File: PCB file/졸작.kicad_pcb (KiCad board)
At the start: 2 copper layers, 7 parts

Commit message: change Pin
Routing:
- net GND: track 239.1 -> 461.2 mm, vias 3 -> 10
- net (no net): track 188.1 -> 18.8 mm, vias 7 -> 1
- net VCC: track 95.5 -> 128.1 mm, vias 0 -> 2

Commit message: Change PCB file
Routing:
- net (no net): track 18.8 -> 66.0 mm, vias 1 -> 0
- net GND: track 461.2 -> 444.9 mm, vias 10 -> 7
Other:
- board text removed: "10"
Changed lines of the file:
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@@
-	)
-	(gr_rect
-		(start 50.1 25.55)
-		(end 51.5 38.05)
-		(stroke
-			(width 0.1)
-			(type solid)
-		)
-		(fill no)
-		(layer "F.SilkS")
-	)
-	(gr_rect
-		(start 52.7 25.55)
-		(end 54.1 38.05)
-		(stroke
-			(width 0.1)
-			(type solid)
-		)
-		(fill no)
-		(layer "F.SilkS")
 	)
 	(gr_rect
@@
 		(layer "F.Paste")
 	)
-	(gr_text "10"
-		(at 52.35 31.625 0)
-		(layer "F.SilkS")
-		(effects
-			(font
-				(size 0.5 0.5)
-				(thickness 0.1)
-			)
-		)
+	(gr_rect
+		(start 49.6 26.2)
+		(end 54.6 29.2)
+		(stroke
+			(width 0.2)
+			(type solid)
+		)
+		(fill yes)
+		(layer "B.Paste")
+	)
+	(gr_rect
+		(start 49.6 30.7)
+		(end 54.6 33.7)
+		(stroke
+			(width 0.2)
+			(type solid)
+		)
+		(fill yes)
+		(layer "B.Paste")
 	)
 	(gr_text "VCC"
@@
 		)
 	)
+	(gr_text_box "PIN0\n"
+		(start 49.95 26.85)
+		(end 54.25 28.6)
+		(margins 1.0025 1.0025 1.0025 1.0025)
+		(layer "F.SilkS")
+		(effects
+			(font
+				(size 1 1)
+				(thickness 0.2)
+				(bold yes)
+			)
+			(justify mirror)
+		)
+		(border yes)
+		(stroke
+			(width 0.1)
+			(type dot)
+		)
+	)
 	(gr_text_box "B-"
 		(start 19.95 41.05)
@@
 		)
 	)
+	(gr_text_box "C-PWM"
+		(start 48.8 31.35)
+		(end 54.6 33.1)
+		(margins 1.0025 1.0025 1.0025 1.0025)
+		(layer "F.SilkS")
+		(effects
+			(font
+				(size 1 1)
+				(thickness 0.2)
+				(bold yes)
+			)
+			(justify mirror)
+		)
+		(border yes)
+		(stroke
+			(width 0.1)
+			(type dot)
+		)
+	)
 	(gr_text_box "4.2V"
 		(start 20 45.05)
@@
 		)
 	)
+	(gr_text_box "Pin2"
+		(start 23.5 19.05)
+		(end 28.25 20.8)
+		(margins 1.0025 1.0025 1.0025 1.0025)
+		(layer "B.SilkS")
+		(effects
+			(font
+				(size 1 1)
+				(thickness 0.1)
+				(italic yes)
+			)
+			(justify mirror)
+		)
+		(border yes)
+		(stroke
+			(width 0.1)
+			(type dot)
+		)
+	)
 	(gr_text_box "Pin1"
 		(start 49.775 9.825)
@@
 		)
 	)
+	(gr_text_box "Pin2"
+		(start 23.5 21.65)
+		(end 28.25 23.4)
+		(margins 1.0025 1.0025 1.0025 1.0025)
+		(layer "B.SilkS")
+		(effects
+			(font
+				(size 1 1)
+				(thickness 0.1)
+				(italic yes)
+			)
+			(justify mirror)
+		)
+		(border yes)
+		(stroke
+			(width 0.1)
+			(type dot)
+		)
+	)
 	(gr_text_box "VCC 5V\n"
 		(start 49.975 1.3)
@@
 		)
 	)
+	(gr_text_box "C-PWM"
+		(start 16 19.1)
+		(end 21.6 20.8)
+		(margins 1.0025 1.0025 1.0025 1.0025)
+		(layer "B.SilkS")
+		(effects
+			(font
+				(size 1 1)
+				(thickness 0.2)
+				(bold yes)
+			)
+			(justify mirror)
+		)
+		(border yes)
+		(stroke
+			(width 0.1)
+			(type dot)
+		)
+	)
 	(gr_text_box "PWM1\n"
 		(start 50.05 18.225)
@@
 	)
 	(gr_text_box "PWM2\n"
-		(start 15.9 24.05)
-		(end 20.2 25.8)
+		(start 18.45 24.05)
+		(end 22.75 25.8)
 		(margins 1.0025 1.0025 1.0025 1.0025)
 		(layer "B.SilkS")
@@
 	)
 	(segment
-		(start 53.4 37.4)
-		(end 53.4 39.4)
-		(width 0.2)
-		(layers "F.Cu" "F.Mask")
-		(net 0)
-	)
-	(via
-		(at 53.4 37.4)
-		(size 1.2)
-		(drill 1)
-		(layers "F.Cu" "B.Cu")
-		(net 0)
-	)
-	(segment
 		(start 37.525 3.9)
 		(end 37.525 9.595)
@@
 		(start 37.525 9.595)
 		(end 29.7 17.42)
+		(width 0.2)
+		(layers "B.Cu" "B.Mask")
+		(net 0)
+	)
+	(segment
+		(start 14.46 19.96)
+		(end 12.64 19.96)
+		(width 0.2)
+		(layers "B.Cu" "B.Mask")
+		(net 0)
+	)
+	(segment
+		(start 11.9 20.7)
+		(end 11.9 26.2)
+		(width 0.2)
+		(layers "B.Cu" "B.Mask")
+		(net 0)
+	)
+	(segment
+		(start 12.64 19.96)
+		(end 11.9 20.7)
+		(width 0.2)
+		(layers "B.Cu" "B.Mask")
+		(net 0)
+	)
+	(segment
+		(start 17.9 32.2)
+		(end 50.3 32.2)
+		(width 0.2)
+		(layers "B.Cu" "B.Mask")
+		(net 0)
+	)
+	(segment
+		(start 11.9 26.2)
+		(end 17.9 32.2)
 		(width 0.2)
 		(layers "B.Cu" "B.Mask")
@@
 	)
 	(segment
-		(start 50.8 37.4)
-		(end 50.925 37.525)
-		(width 0.2)
-		(layers "F.Cu" "F.Mask")
-		(net 5)
-	)
-	(segment
 		(start 10.83 3.16)
 		(end 23.06 3.16)
@@
 	)
 	(segment
-		(start 50.8 26.2)
-		(end 53.4 26.2)
-		(width 0.2)
-		(layers "F.Cu" "F.Mask")
-		(net 5)
-	)
-	(segment
 		(start 12.875 43.257673)
 		(end 12.140346 43.257673)
@@
 		(width 0.2)
 		(layers "F.Cu" "F.Mask")
-		(net 5)
-	)
-	(via
-		(at 53.4 26.2)
-		(size 1.2)
-		(drill 1)
-		(layers "F.Cu" "B.Cu")
-		(net 5)
-	)
-	(via
-		(at 50.8 37.4)
-		(size 1.2)
-		(drill 1)
-		(layers "F.Cu" "B.Cu")
 		(net 5)
 	)
@@
 	)
 	(via
-		(at 50.8 26.2)
-		(size 1.2)
-		(drill 1)
-		(layers "F.Cu" "B.Cu")
-		(net 5)
-	)
-	(via
 		(at 42.55 29.525)
 		(size 0.6)
@@
 	)
 	(segment
-		(start 33.225 24.975)
-		(end 29.765 24.975)
-		(width 0.2)
-		(layers "B.Cu" "B.Mask")
-		(net 5)
-	)
-	(segment
-		(start 37.4 37.4)
-		(end 50.8 37.4)
-		(width 0.2)
-		(layers "B.Cu" "B.Mask")
-		(net 5)
-	)
-	(segment
-		(start 34.45 26.2)
-		(end 33.225 24.975)
-		(width 0.2)
-		(layers "B.Cu" "B.Mask")
-		(net 5)
-	)
-	(segment
-		(start 50.8 26.2)
-		(end 34.45 26.2)
-		(width 0.2)
-		(layers "B.Cu" "B.Mask")
-		(net 5)
-	)
-	(segment
 		(start 39 19.96)
 		(end 29.7 19.96)
@@
 		(start 33.525 8.05)
 		(end 33.525 4)
+		(width 0.2)
+		(layers "B.Cu" "B.Mask")
+		(net 5)
+	)
+	(segment
+		(start 50 27.7)
+		(end 35.95 27.7)
 		(width 0.2)
 		(layers "B.Cu" "B.Mask")
@@
 		(net 5)
 	)
+	(segment
+		(start 35.95 27.7)
+		(end 33.225 24.975)
+		(width 0.2)
+		(layers "B.Cu" "B.Mask")
+		(net 5)
+	)
+	(segment
+		(start 33.225 24.975)
+		(end 29.765 24.975)
+		(width 0.2)
+		(layers "B.Cu" "B.Mask")
+		(net 5)
+	)

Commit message: Add files via upload
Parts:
- added ?: , , F.Cu at (53.0, 19.9)
- added ?: , , F.Cu at (21.6, 52.6)
- added ?: , , F.Cu at (53.0, 27.8)
- added ?: , , F.Cu at (52.9, 1.85)
- added ?: , , F.Cu at (52.9, 5.28)
- added ?: , , F.Cu at (53.0, 32.2)
- added ?: , , F.Cu at (21.6, 40.0)
- added ?: , , F.Cu at (52.9, 8.70)
- added ?: , , F.Cu at (52.5, 40.0)
- added PAD: F_MASK SMD PAD, PAD:F_MASK SMD PAD, F.Cu at (53.0, 15.9)
- added PAD: F_MASK SMD PAD, PAD:F_MASK SMD PAD, F.Cu at (53.0, 12.1)
- added PAD: F_MASK SMD PAD, PAD:F_MASK SMD PAD, F.Cu at (53.0, 23.6)
- added PAD: F_MASK SMD PAD, PAD:F_MASK SMD PAD, F.Cu at (52.5, 52.6)
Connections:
- Button pad 1: (no net) -> GND
- Button pad 2: (no net) -> VCC
- Button pad 3: (no net) -> BOOT
- Button pad 4: (no net) -> UP
- Button pad 5: (no net) -> DOWN
- Display / I2C Bus pad 1: (no net) -> GND
- Display / I2C Bus pad 2: (no net) -> VCC
- Display / I2C Bus pad 3: (no net) -> SDA
- Display / I2C Bus pad 4: (no net) -> SCL
- ESP32-C3 SuperMini pad 0: (no net) -> feltier1
- ESP32-C3 SuperMini pad 1: (no net) -> COOLER_PIN
- ESP32-C3 SuperMini pad 10: (no net) -> COOLING
- ESP32-C3 SuperMini pad 2: (no net) -> HEATER_PIN
- ESP32-C3 SuperMini pad 20: (no net) -> feltier2
- ESP32-C3 SuperMini pad 21: (no net) -> ACTIVEPIN
- ESP32-C3 SuperMini pad 3: (no net) -> HPIN
- ESP32-C3 SuperMini pad 3.3: (no net) -> VCC
- ESP32-C3 SuperMini pad 4: (no net) -> Sensors
- ESP32-C3 SuperMini pad 5: (no net) -> BOOT
- ESP32-C3 SuperMini pad 6: (no net) -> UP
- ESP32-C3 SuperMini pad 7: (no net) -> DOWN
- ESP32-C3 SuperMini pad 8: (no net) -> SDA
- ESP32-C3 SuperMini pad 9: (no net) -> SCL
- ESP32-C3 SuperMini pad G: (no net) -> GND
- Sensors pad 1: (no net) -> Sensors
- Sensors pad 2: (no net) -> VCC
- Sensors pad 3: (no net) -> GND
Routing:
- net GND: track 444.9 -> 181.7 mm, vias 7 -> 2
- net 5V: track 0.00 -> 72.6 mm
- net (no net): track 66.0 -> 0.00 mm
- net COOLING: track 0.00 -> 52.0 mm
- net feltier2: track 0.00 -> 51.2 mm, vias 0 -> 1
- net ACTIVEPIN: track 0.00 -> 46.9 mm, vias 0 -> 1
- net COOLER_PIN: track 0.00 -> 30.9 mm, vias 0 -> 1
- net HEATER_PIN: track 0.00 -> 29.1 mm, vias 0 -> 1
- net HPIN: track 0.00 -> 26.5 mm, vias 0 -> 1
- net feltier1: track 0.00 -> 24.4 mm
- net Sensors: track 0.00 -> 14.2 mm
- net BOOT: track 0.00 -> 9.00 mm
- net UP: track 0.00 -> 8.77 mm
- net DOWN: track 0.00 -> 8.55 mm
- net VCC: track 128.1 -> 128.8 mm
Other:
- board outline added: 55 x 55 mm

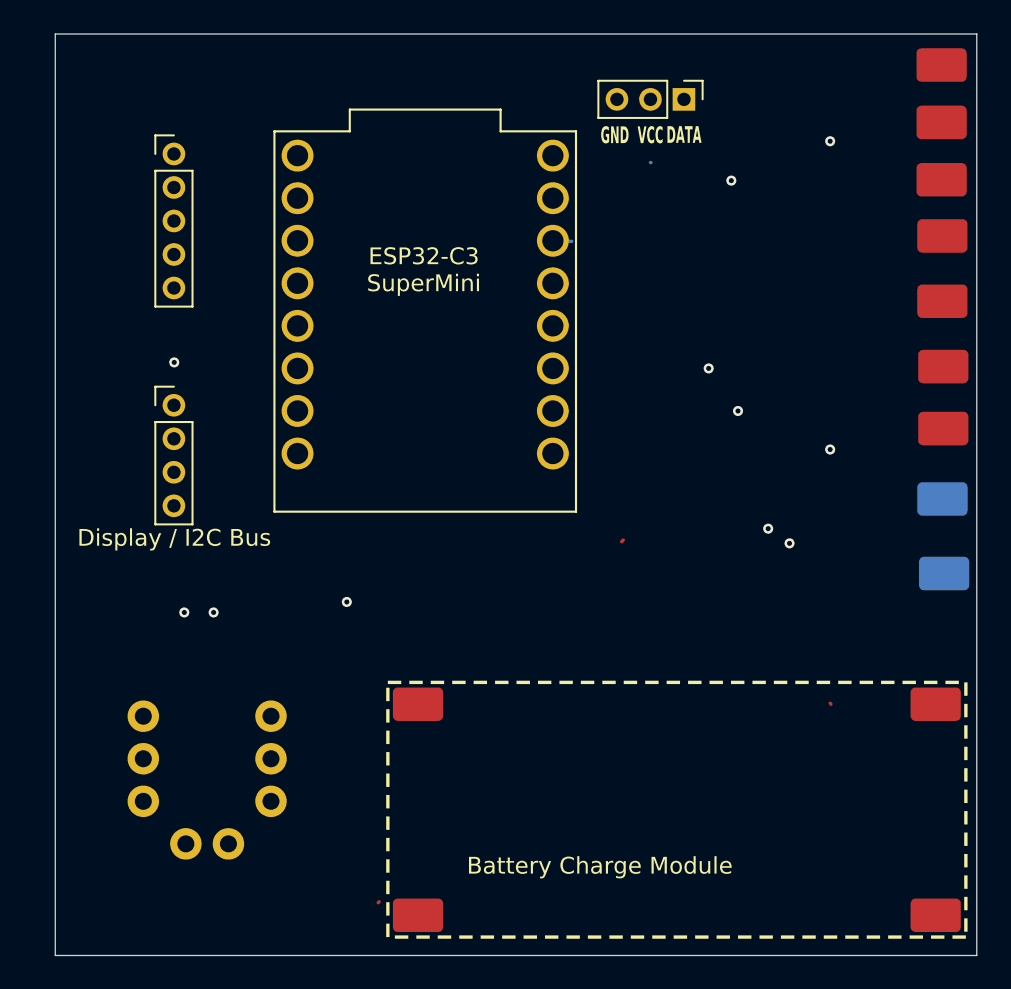
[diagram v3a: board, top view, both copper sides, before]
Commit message: Update size 40 x 50
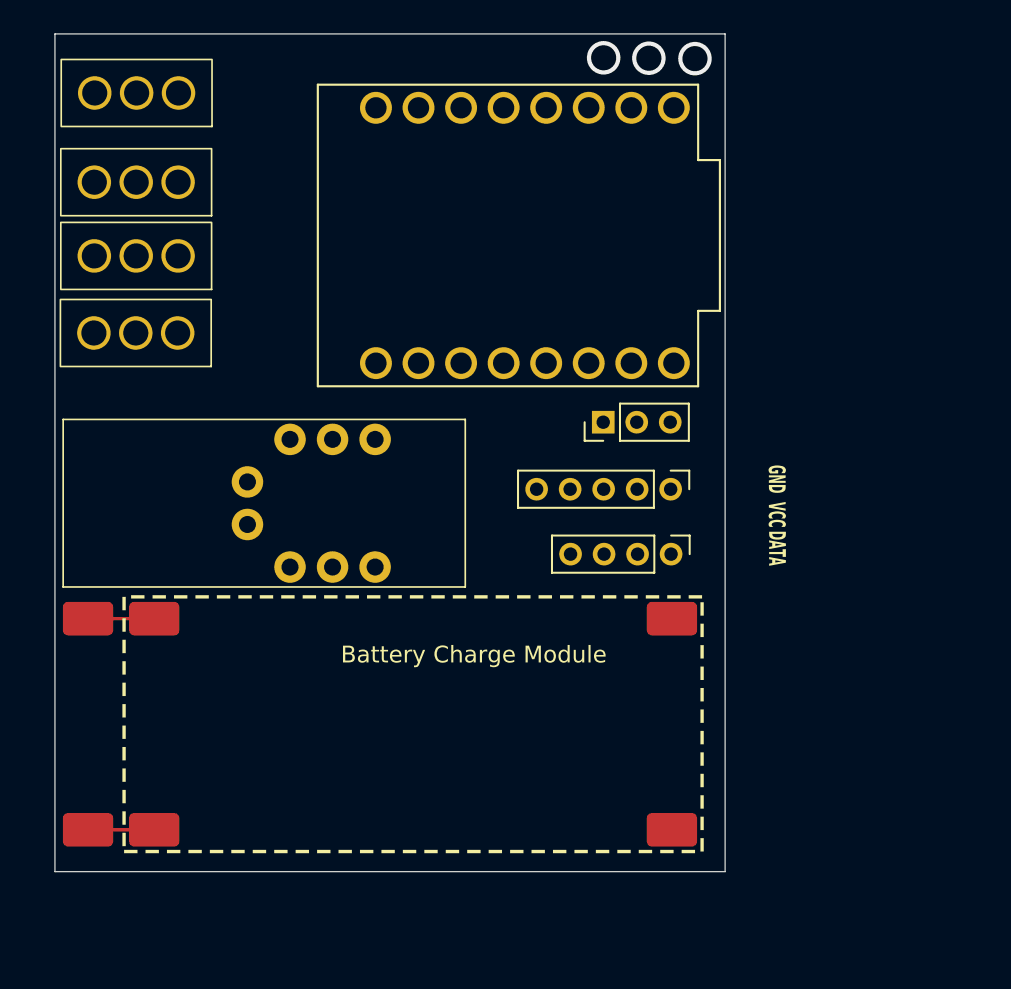
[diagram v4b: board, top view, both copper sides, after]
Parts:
- removed the ? at (53.0, 19.9)
- removed the ? at (53.0, 27.8)
- removed the ? at (53.0, 32.2)
- removed the ? at (52.9, 8.70)
- removed the PAD at (53.0, 15.9)
- removed the PAD at (53.0, 12.1)
- removed the PAD at (53.0, 23.6)
- added REF**: IRL540N, mosfet:IRL540N, F.Cu at (4.86, 3.52)
- added REF**: IRL540N, mosfet:IRL540N, F.Cu at (4.80, 17.8)
- added REF**: IRL540N, mosfet:IRL540N, F.Cu at (4.83, 13.2)
- added REF**: IRL540N, mosfet:IRL540N, F.Cu at (4.83, 8.85)
- moved ? 68.4 mm to (1.96, 47.5)
- moved ? 58.9 mm to (1.96, 34.9)
- moved Button 35.8 mm to (36.7, 27.2), turned to -90 degrees
- moved Display / I2C Bus 31.0 mm to (36.8, 31.0), turned to -90 degrees
- moved JP2 23.3 mm to (14.0, 24.2), turned to 0 degrees
- moved JP5 21.9 mm to (11.5, 26.7), turned to -90 degrees
- moved Sensors 19.9 mm to (32.7, 23.2), turned to 90 degrees
- moved ? 16.6 mm to (5.91, 47.5)
- moved ? 16.6 mm to (5.91, 34.9)
- moved ? 16.6 mm to (36.8, 34.9)
- moved PAD 16.6 mm to (36.8, 47.5)
- moved JP4 14.0 mm to (14.0, 31.8), turned to 0 degrees
- moved ESP32-C3 SuperMini 7.13 mm to (27.0, 12.0), turned to -90 degrees
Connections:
- ? pad A: VCC -> 5V
- ESP32-C3 SuperMini pad 0: feltier1 -> ACTIVEPIN
- ESP32-C3 SuperMini pad 1: COOLER_PIN -> DOWN
- ESP32-C3 SuperMini pad 10: COOLING -> feltier3
- ESP32-C3 SuperMini pad 2: HEATER_PIN -> UP
- ESP32-C3 SuperMini pad 21: ACTIVEPIN -> feltier1
- ESP32-C3 SuperMini pad 3: HPIN -> BOOT
- ESP32-C3 SuperMini pad 5: BOOT -> COOLER_PIN
- ESP32-C3 SuperMini pad 5V: (no net) -> VCC
- ESP32-C3 SuperMini pad 6: UP -> HEATER_PIN
- ESP32-C3 SuperMini pad 7: DOWN -> COOLING
- PAD pad A: 5V -> VCC
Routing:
- net GND: track 181.7 -> 43.8 mm, vias 2 -> 0
- net 5V: track 72.6 -> 3.95 mm
- net VCC: track 128.8 -> 76.8 mm, vias 2 -> 0
- net feltier2: track 51.2 -> 18.5 mm, vias 1 -> 0
- net COOLER_PIN: track 30.9 -> 3.58 mm
- net HPIN: track 26.5 -> 0.00 mm, vias 1 -> 0
- net HEATER_PIN: track 29.1 -> 3.67 mm
- net COOLING: track 52.0 -> 26.6 mm
- net feltier3: track 0.00 -> 22.5 mm
- net ACTIVEPIN: track 46.9 -> 29.6 mm
- net SCL: track 33.3 -> 50.1 mm, vias 1 -> 0
- net feltier1: track 24.4 -> 13.8 mm
- net Sensors: track 14.2 -> 4.94 mm
- net SDA: track 39.4 -> 46.4 mm, vias 1 -> 0
- net DOWN: track 8.55 -> 10.4 mm
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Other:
- board size 55 x 55 mm -> 40 x 50 mm

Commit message: Add files via upload
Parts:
- removed Button: PinHeader_1x05_P2.00mm_Vertical, Connector_PinHeader_2.00mm:PinHeader_1x05_P2.00mm_Vertical
- removed Display / I2C Bus: PinHeader_1x04_P2.00mm_Vertical, Connector_PinHeader_2.00mm:PinHeader_1x04_P2.00mm_Vertical
- removed Sensors: PinHeader_1x03_P2.00mm_Vertical, Connector_PinHeader_2.00mm:PinHeader_1x03_P2.00mm_Vertical
- moved REF** 93.2 mm to (60.3, 78.4)
- moved ? 93.2 mm to (61.3, 122.4)
- moved ? 93.2 mm to (57.4, 122.4)
- moved ? 93.2 mm to (57.4, 109.8)
- moved ? 93.2 mm to (61.3, 109.8)
- moved ? 93.2 mm to (92.2, 109.8)
- moved ESP32-C3 SuperMini 93.2 mm to (82.4, 86.9)
- moved JP2 93.2 mm to (69.4, 99.1)
- moved JP4 93.2 mm to (69.4, 106.7)
- moved JP5 93.2 mm to (66.9, 101.6)
- moved PAD 93.2 mm to (92.2, 122.4)
- moved REF** 93.2 mm to (60.2, 92.7)
- moved REF** 93.2 mm to (60.2, 88.1)
- moved REF** 93.2 mm to (60.2, 83.7)
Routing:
- net GND: track 43.8 -> 42.0 mm, vias 0 -> 3
- net VCC: track 76.8 -> 78.0 mm, vias 0 -> 3
- net Sensors: track 4.94 -> 6.05 mm, vias 0 -> 1
- net BOOT: track 10.00 -> 10.7 mm, vias 0 -> 1
- net SCL: track 50.1 -> 49.4 mm, vias 0 -> 1
- net UP: track 10.2 -> 9.90 mm, vias 0 -> 1
- net SDA: track 46.4 -> 46.2 mm, vias 0 -> 1
- net DOWN: vias 0 -> 1
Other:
- board text removed: "DATA"
- board text removed: "GND"
- board text removed: "VCC"
